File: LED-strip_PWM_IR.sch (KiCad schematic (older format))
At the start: 13 parts, among them IC1 ATtiny85, P1 CONN_2, P2 CONN_2, Q1 8MHz, T1 IRLR2905_DPAK, U1 TSOP38238, U2 7805MS

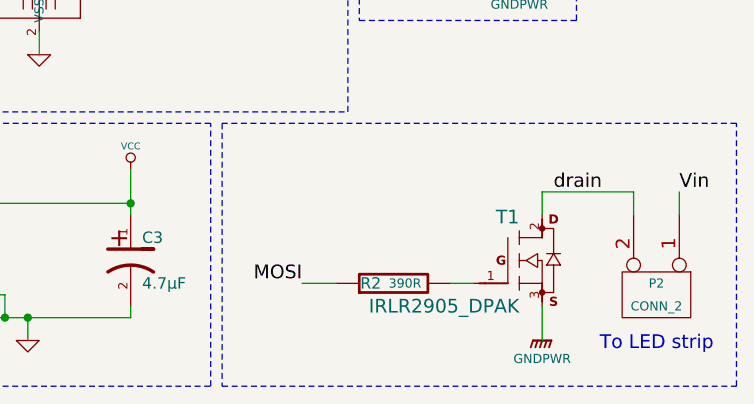
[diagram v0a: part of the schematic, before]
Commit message: Changed IRLR2905 gate resistor to 150R.
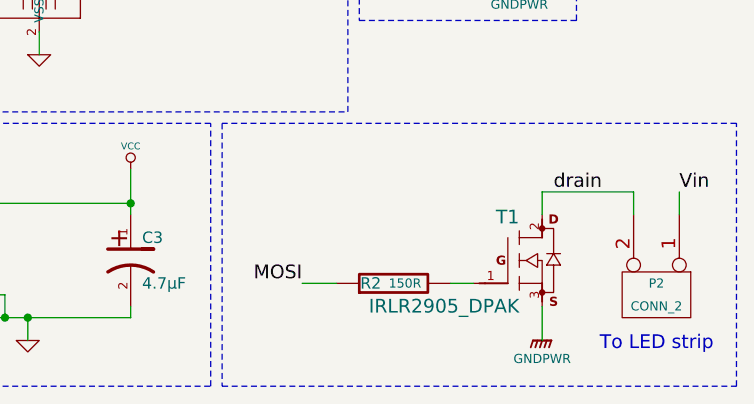
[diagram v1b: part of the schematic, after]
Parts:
- R2: value 390R -> 150R
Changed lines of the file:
@@
-EESchema Schematic File Version 2  date Sun 25 Nov 2012 02:49:51 PM CET
+EESchema Schematic File Version 2  date Mon 26 Nov 2012 02:29:05 PM CET
 LIBS:my_parts
 LIBS:power
@@
 Sheet 1 1
 Title "LED-strip_PWM_IR"
-Date "25 nov 2012"
+Date "26 nov 2012"
 Rev "0.1"
 Comp "2012 - blog.spitzenpfeil.org"
@@
 P 5350 3750
 F 0 "R2" V 5350 3850 50  0000 C CNN
-F 1 "390R" V 5350 3700 40  0000 C CNN
+F 1 "150R" V 5350 3700 40  0000 C CNN
 	1    5350 3750
 	0    -1   -1   0

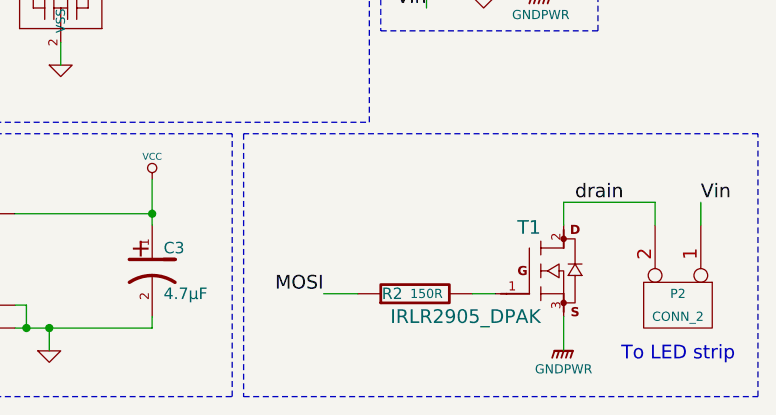
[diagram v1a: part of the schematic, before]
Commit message: Added a 20k gate pull-down.
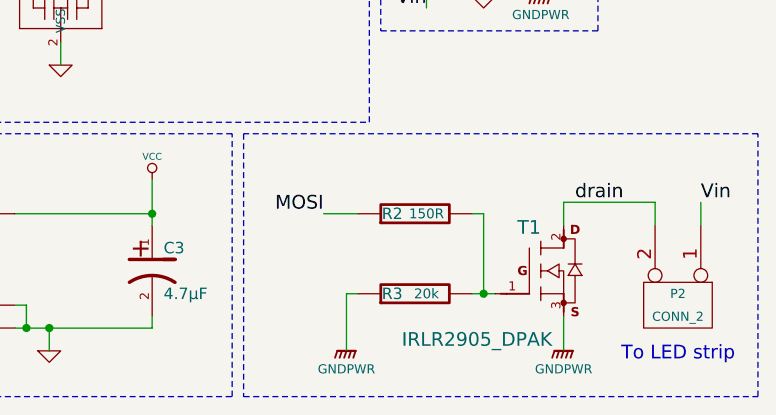
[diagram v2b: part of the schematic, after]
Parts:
- added R3: 20k, symbol R
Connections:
- net GNDPWR: now also R3.1
- net at R2.2, T1.1 (G): now also R3.2
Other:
- moved on the sheet: R2
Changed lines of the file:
@@
-EESchema Schematic File Version 2  date Mon 26 Nov 2012 02:29:05 PM CET
+EESchema Schematic File Version 2  date Tue 27 Nov 2012 09:08:00 PM CET
 LIBS:my_parts
 LIBS:power
@@
 Sheet 1 1
 Title "LED-strip_PWM_IR"
-Date "26 nov 2012"
-Rev "0.1"
+Date "27 nov 2012"
+Rev "0.11"
 Comp "2012 - blog.spitzenpfeil.org"
 Comment1 ""
@@
 L R R2
 U 1 1 4F6EEBD3
-P 5350 3750
-F 0 "R2" V 5350 3850 50  0000 C CNN
-F 1 "150R" V 5350 3700 40  0000 C CNN
-	1    5350 3750
+P 5350 3400
+F 0 "R2" V 5350 3500 50  0000 C CNN
+F 1 "150R" V 5350 3350 43  0000 C CNN
+	1    5350 3400
 	0    -1   -1   0
 $EndComp
@@
 P 5700 3750
 F 0 "T1" H 5900 4040 60  0000 R CNN
-F 1 "IRLR2905_DPAK" H 5900 3650 60  0000 R CNN
+F 1 "IRLR2905_DPAK" H 5950 3550 60  0000 R CNN
 	1    5700 3750
 	1    0    0    -1
 $EndComp
 Connection ~ 1450 1650
-Text Label 4950 3750 2    60   ~ 0
+Text Label 4950 3400 2    60   ~ 0
 MOSI
 $Comp
@@
 Wire Wire Line
 	1350 1650 1600 1650
-Wire Wire Line
-	5600 3750 5700 3750
-Wire Wire Line
-	4950 3750 5100 3750
 $Comp
 L CONN_2 P2
@@
 Text Label 6050 3350 0    60   ~ 0
 drain
+Wire Wire Line
+	4950 3400 5100 3400
+Wire Wire Line
+	5600 3400 5650 3400
+Wire Wire Line
+	5650 3400 5650 3750
+Wire Wire Line
+	5600 3750 5700 3750
+$Comp
+L R R3
+U 1 1 50B51D62
+P 5350 3750
+F 0 "R3" V 5350 3850 50  0000 C CNN
+F 1 "20k" V 5350 3700 43  0000 C CNN
+	1    5350 3750
+	0    -1   -1   0
+$EndComp
+Connection ~ 5650 3750
+Wire Wire Line
+	5100 3750 5050 3750
+Wire Wire Line
+	5050 3750 5050 4000
+$Comp
+L GNDPWR #PWR018
+U 1 1 50B51E71
+P 5050 4000
+F 0 "#PWR018" H 5050 4050 40  0001 C CNN
+F 1 "GNDPWR" H 5050 3920 40  0000 C CNN
+	1    5050 4000
+	1    0    0    -1
+$EndComp
 $EndSCHEMATC

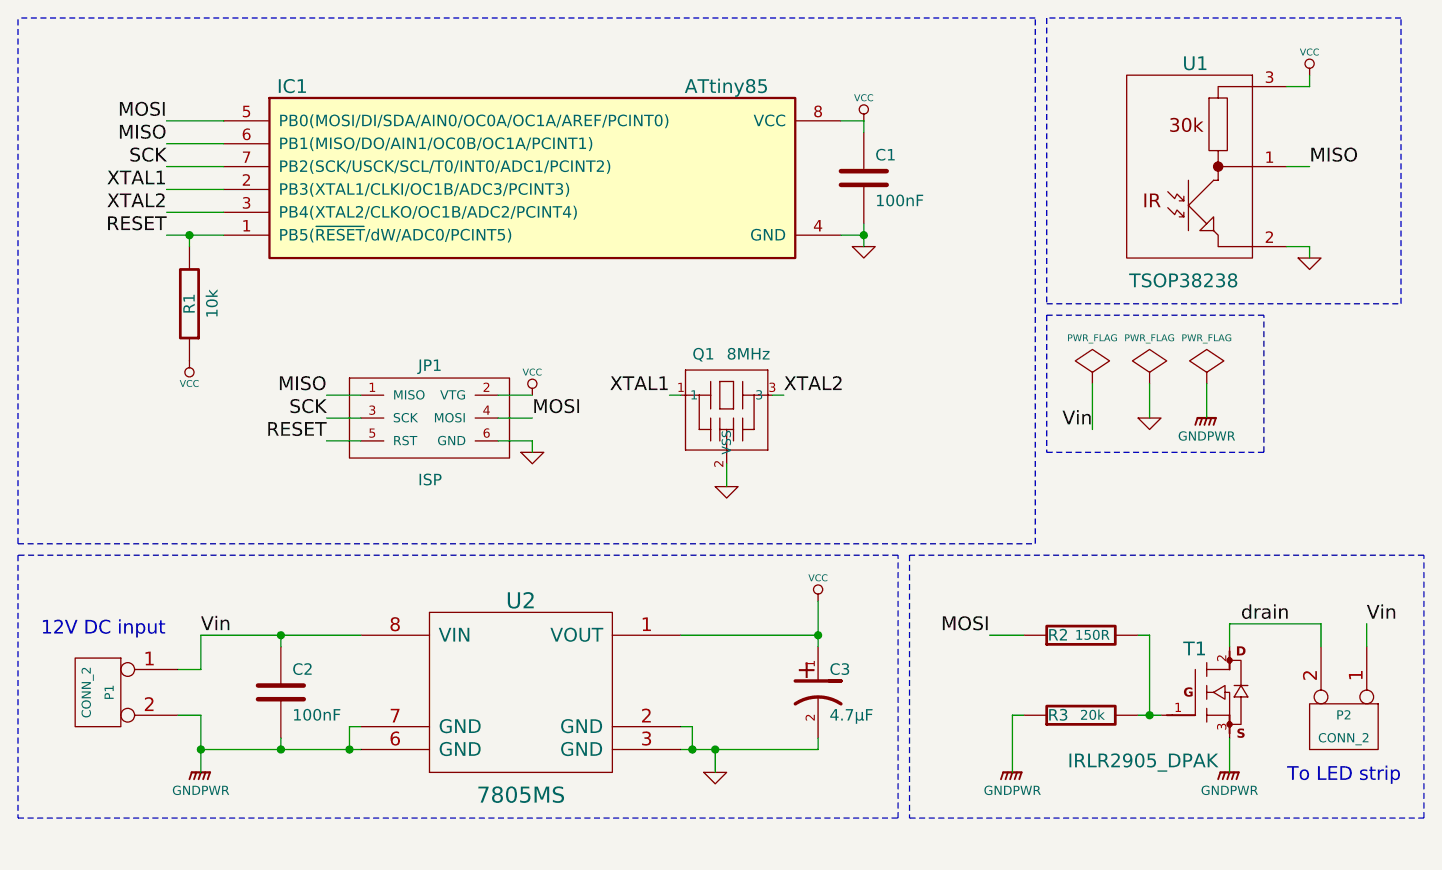
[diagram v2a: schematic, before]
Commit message: Replaced 78L05 with MCP1804-SOT23 (low drop). Board-shrink.
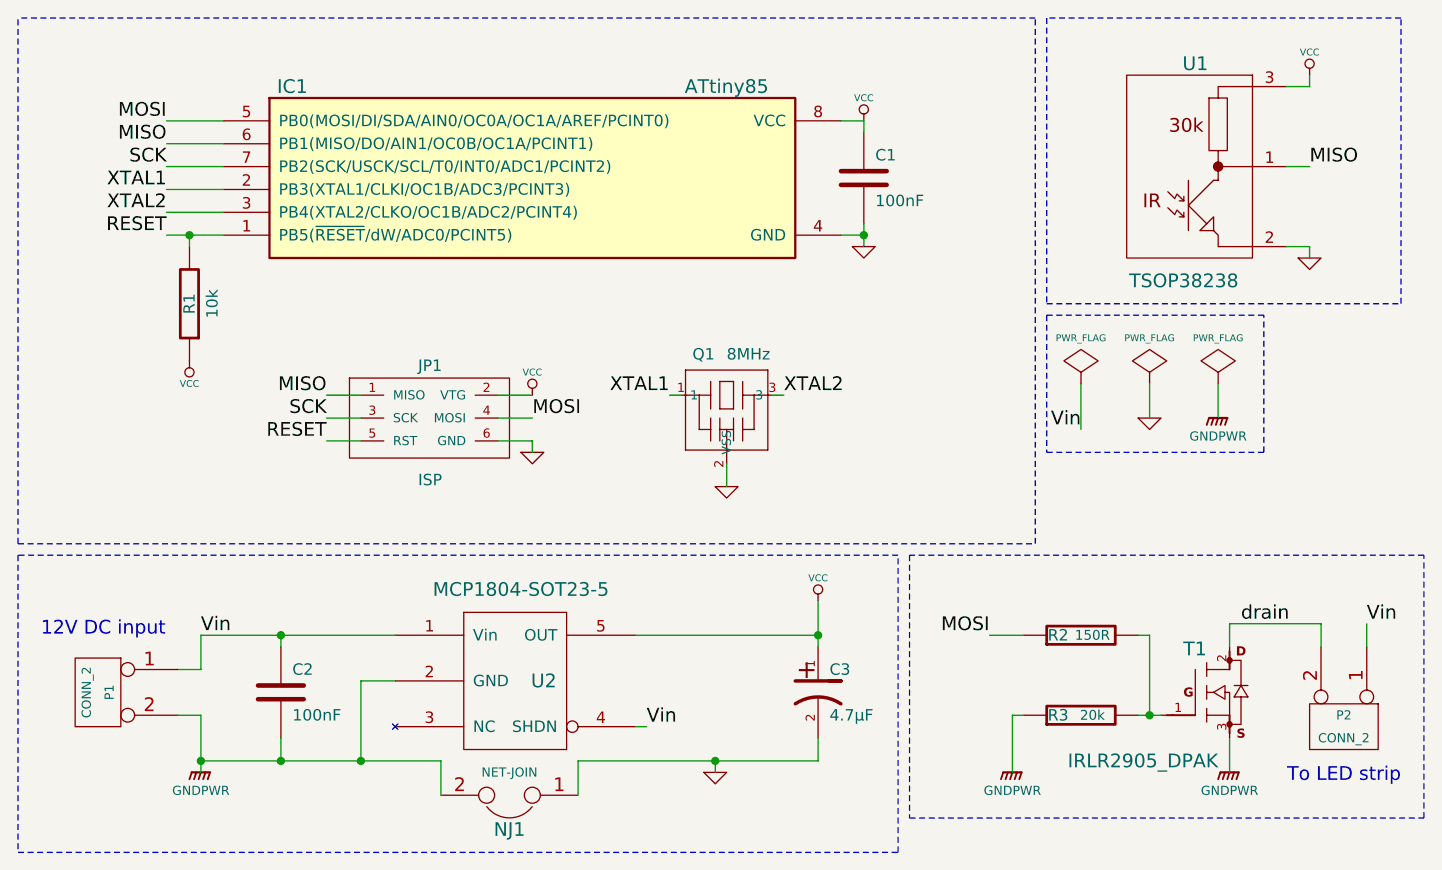
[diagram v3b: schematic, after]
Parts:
- removed U2: 7805MS, symbol 7805MS
- added NJ1: NET-JOIN, symbol JUMPER
- added U2: MCP1804-SOT23-5, symbol MADW__MCP1804-SOT23-5
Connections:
- net GND: now also NJ1.1
- net GNDPWR: now also NJ1.2, U2.2 (GND)
- net VCC: now also U2.5 (OUT)
- net Vin: now also U2.1 (Vin), U2.4 (SHDN)
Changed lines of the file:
@@
-EESchema Schematic File Version 2  date Tue 27 Nov 2012 09:08:00 PM CET
+EESchema Schematic File Version 2  date Wed 09 Jan 2013 04:06:11 PM CET
 LIBS:my_parts
 LIBS:power
@@
 EELAYER 27 0
 EELAYER END
-$Descr User 8268 5866
+$Descr User 8268 5906
 encoding utf-8
 Sheet 1 1
 Title "LED-strip_PWM_IR"
-Date "27 nov 2012"
-Rev "0.11"
+Date "9 jan 2013"
+Rev "0.2"
 Comp "2012 - blog.spitzenpfeil.org"
 Comment1 ""
@@
 	5150 700  700  700
 Wire Wire Line
-	4200 3400 3600 3400
+	3400 3400 4200 3400
 $Comp
 L VCC #PWR01
@@
 F 1 "100nF" H 1900 3550 50  0000 L CNN
 	1    1850 3650
-	1    0    0    -1
-$EndComp
-$Comp
-L PWR_FLAG #FLG02
-U 1 1 4F6EE916
-P 5650 2300
-F 0 "#FLG02" H 5650 2570 30  0001 C CNN
-F 1 "PWR_FLAG" H 5650 2500 30  0000 C CNN
-	1    5650 2300
 	1    0    0    -1
 $EndComp
@@
 RESET
 $Comp
-L GND #PWR03
+L GND #PWR02
 U 1 1 4F6EE8F0
 P 6350 1750
-F 0 "#PWR03" H 6350 1750 30  0001 C CNN
+F 0 "#PWR02" H 6350 1750 30  0001 C CNN
 F 1 "GND" H 6350 1680 30  0001 C CNN
 	1    6350 1750
@@
 $EndComp
 $Comp
-L VCC #PWR04
+L VCC #PWR03
 U 1 1 4F6EE8E3
 P 6350 950
-F 0 "#PWR04" H 6350 1050 30  0001 C CNN
+F 0 "#PWR03" H 6350 1050 30  0001 C CNN
 F 1 "VCC" H 6350 1050 30  0000 C CNN
 	1    6350 950
@@
 $EndComp
 $Comp
-L VCC #PWR05
+L VCC #PWR04
 U 1 1 4F6EE887
 P 4400 1150
-F 0 "#PWR05" H 4400 1250 30  0001 C CNN
+F 0 "#PWR04" H 4400 1250 30  0001 C CNN
 F 1 "VCC" H 4400 1250 30  0000 C CNN
 	1    4400 1150
@@
 $EndComp
 $Comp
-L GND #PWR06
+L GND #PWR05
 U 1 1 4F6EE882
 P 4400 1700
-F 0 "#PWR06" H 4400 1700 30  0001 C CNN
+F 0 "#PWR05" H 4400 1700 30  0001 C CNN
 F 1 "GND" H 4400 1630 30  0001 C CNN
 	1    4400 1700
@@
 MOSI
 $Comp
-L GND #PWR07
+L GND #PWR06
 U 1 1 4F6EE81E
 P 2950 2600
-F 0 "#PWR07" H 2950 2600 30  0001 C CNN
+F 0 "#PWR06" H 2950 2600 30  0001 C CNN
 F 1 "GND" H 2950 2530 30  0001 C CNN
 	1    2950 2600
@@
 MOSI
 $Comp
-L VCC #PWR08
+L VCC #PWR07
 U 1 1 4F6EE80A
 P 2950 2350
-F 0 "#PWR08" H 2950 2450 30  0001 C CNN
+F 0 "#PWR07" H 2950 2450 30  0001 C CNN
 F 1 "VCC" H 2950 2450 30  0000 C CNN
 	1    2950 2350
@@
 XTAL2
 $Comp
-L GND #PWR09
+L GND #PWR08
 U 1 1 4F6EE7AB
 P 3800 2750
-F 0 "#PWR09" H 3800 2750 30  0001 C CNN
+F 0 "#PWR08" H 3800 2750 30  0001 C CNN
 F 1 "GND" H 3800 2680 30  0001 C CNN
 	1    3800 2750
@@
 $EndComp
 $Comp
-L VCC #PWR010
+L VCC #PWR09
 U 1 1 4F6EE70F
 P 1450 2200
-F 0 "#PWR010" H 1450 2300 30  0001 C CNN
+F 0 "#PWR09" H 1450 2300 30  0001 C CNN
 F 1 "VCC" H 1450 2300 30  0000 C CNN
 	1    1450 2200
@@
 $EndComp
 $Comp
-L PWR_FLAG #FLG011
+L PWR_FLAG #FLG010
 U 1 1 50B1E380
-P 5400 2300
-F 0 "#FLG011" H 5400 2395 30  0001 C CNN
-F 1 "PWR_FLAG" H 5400 2500 30  0000 C CNN
-	1    5400 2300
-	1    0    0    -1
-$EndComp
-$Comp
-L 7805MS U2
-U 1 1 50B1E462
-P 2900 3650
-F 0 "U2" H 2900 4050 70  0000 C CNN
-F 1 "7805MS" H 2900 3200 70  0000 C CNN
-	1    2900 3650
-	1    0    0    -1
-$EndComp
-Wire Wire Line
-	1500 3900 2200 3900
-Wire Wire Line
-	2200 3800 2150 3800
-Wire Wire Line
-	2150 3800 2150 3900
-Connection ~ 2150 3900
-Wire Wire Line
-	3600 3900 4200 3900
-Connection ~ 3650 3900
+P 5350 2300
+F 0 "#FLG010" H 5350 2395 30  0001 C CNN
+F 1 "PWR_FLAG" H 5350 2500 30  0000 C CNN
+	1    5350 2300
+	1    0    0    -1
+$EndComp
 Connection ~ 4200 3400
 Wire Wire Line
-	4200 3900 4200 3850
-Wire Notes Line
-	4550 4200 4550 3050
+	4200 3950 4200 3850
 $Comp
 L MADW__IRLZ34N T1
@@
 MOSI
 $Comp
-L GNDPWR #PWR012
+L GNDPWR #PWR011
 U 1 1 50B209CF
 P 6000 4000
-F 0 "#PWR012" H 6000 4050 40  0001 C CNN
+F 0 "#PWR011" H 6000 4050 40  0001 C CNN
 F 1 "GNDPWR" H 6000 3920 40  0000 C CNN
 	1    6000 4000
@@
 	6750 1950 6750 700
 Wire Wire Line
-	1500 3400 2200 3400
+	1500 3400 2350 3400
 Wire Wire Line
 	1400 3750 1500 3750
 Wire Wire Line
 	1500 3750 1500 4000
-Connection ~ 1850 3900
 Wire Wire Line
 	1400 3550 1500 3550
@@
 	1500 3550 1500 3400
 Connection ~ 1850 3400
-Connection ~ 1500 3900
-$Comp
-L GND #PWR013
-U 1 1 50B21224
-P 3750 4000
-F 0 "#PWR013" H 3750 4000 30  0001 C CNN
-F 1 "GND" H 3750 3930 30  0001 C CNN
-	1    3750 4000
-	1    0    0    -1
-$EndComp
-Wire Wire Line
-	3600 3800 3650 3800
-Wire Wire Line
-	3650 3800 3650 3900
 Wire Wire Line
 	1850 3450 1850 3400
 Wire Wire Line
-	1850 3900 1850 3850
+	1850 3850 1850 3950
+$Comp
+L GNDPWR #PWR012
+U 1 1 50B2137E
+P 5950 2450
+F 0 "#PWR012" H 5950 2500 40  0001 C CNN
+F 1 "GNDPWR" H 5950 2370 40  0000 C CNN
+	1    5950 2450
+	1    0    0    -1
+$EndComp
+Wire Notes Line
+	4550 3050 700  3050
+$Comp
+L PWR_FLAG #FLG013
+U 1 1 50B2144E
+P 5950 2300
+F 0 "#FLG013" H 5950 2395 30  0001 C CNN
+F 1 "PWR_FLAG" H 5950 2500 30  0000 C CNN
+	1    5950 2300
+	1    0    0    -1
+$EndComp
+Text Label 5350 2500 2    60   ~ 0
+Vin
+Wire Wire Line
+	5950 2300 5950 2450
+Wire Wire Line
+	5350 2300 5350 2500
+Wire Notes Line
+	5200 2000 5200 2600
+Wire Notes Line
+	5200 2600 6150 2600
+Wire Notes Line
+	6150 2600 6150 2000
+Wire Notes Line
+	6150 2000 5200 2000
 $Comp
 L GNDPWR #PWR014
-U 1 1 50B2137E
-P 5900 2450
-F 0 "#PWR014" H 5900 2500 40  0001 C CNN
-F 1 "GNDPWR" H 5900 2370 40  0000 C CNN
-	1    5900 2450
-	1    0    0    -1
-$EndComp
-Wire Notes Line
-	4550 3050 700  3050
-Wire Notes Line
-	700  3050 700  4200
-Wire Notes Line
-	700  4200 4550 4200
-$Comp
-L PWR_FLAG #FLG015
-U 1 1 50B2144E
-P 5900 2300
-F 0 "#FLG015" H 5900 2395 30  0001 C CNN
-F 1 "PWR_FLAG" H 5900 2500 30  0000 C CNN
-	1    5900 2300
-	1    0    0    -1
-$EndComp
-$Comp
-L GND #PWR016
-U 1 1 50B2147B
-P 5650 2450
-F 0 "#PWR016" H 5650 2450 30  0001 C CNN
-F 1 "GND" H 5650 2380 30  0001 C CNN
-	1    5650 2450
-	1    0    0    -1
-$EndComp
-Text Label 5400 2500 2    60   ~ 0
-Vin
-Wire Wire Line
-	5900 2300 5900 2450
-Wire Wire Line
-	5650 2300 5650 2450
-Wire Wire Line
-	5400 2300 5400 2500
-Wire Notes Line
-	5200 2000 5200 2600
-Wire Notes Line
-	5200 2600 6150 2600
-Wire Notes Line
-	6150 2600 6150 2000
-Wire Notes Line
-	6150 2000 5200 2000
-$Comp
-L GNDPWR #PWR017
 U 1 1 50B216E0
 P 1500 4000
-F 0 "#PWR017" H 1500 4050 40  0001 C CNN
+F 0 "#PWR014" H 1500 4050 40  0001 C CNN
 F 1 "GNDPWR" H 1500 3920 40  0000 C CNN
 	1    1500 4000
 	1    0    0    -1
 $EndComp
-Wire Wire Line
-	3750 3900 3750 4000
-Connection ~ 3750 3900
 Text Label 6050 3350 0    60   ~ 0
 drain
@@
 	5050 3750 5050 4000
 $Comp
-L GNDPWR #PWR018
+L GNDPWR #PWR015
 U 1 1 50B51E71
 P 5050 4000
-F 0 "#PWR018" H 5050 4050 40  0001 C CNN
+F 0 "#PWR015" H 5050 4050 40  0001 C CNN
 F 1 "GNDPWR" H 5050 3920 40  0000 C CNN
 	1    5050 4000
 	1    0    0    -1
 $EndComp
+$Comp
+L MADW__MCP1804-SOT23-5 U2
+U 1 1 50ED7AA4
+P 2850 3600
+F 0 "U2" H 3000 3600 60  0000 C CNN
+F 1 "MCP1804-SOT23-5" H 2900 4000 60  0000 C CNN
+	1    2850 3600
+	1    0    0    -1
+$EndComp
+Connection ~ 1500 3950
+Wire Wire Line
+	2350 3600 2200 3600
+Wire Wire Line
+	2200 3600 2200 3950
+Connection ~ 2200 3950
+Connection ~ 1850 3950
+Connection ~ 3750 3950
+$Comp
+L GND #PWR016
+U 1 1 50B21224
+P 3750 4000
+F 0 "#PWR016" H 3750 4000 30  0001 C CNN
+F 1 "GND" H 3750 3930 30  0001 C CNN
+	1    3750 4000
+	1    0    0    -1
+$EndComp
+Wire Wire Line
+	3750 3950 3750 4000
+Text Label 3450 3800 0    60   ~ 0
+Vin
+Wire Wire Line
+	3400 3800 3450 3800
+$Comp
+L JUMPER NJ1
+U 1 1 50ED7F02
+P 2850 4100
+F 0 "NJ1" H 2850 4250 60  0000 C CNN
+F 1 "NET-JOIN" H 2850 4000 40  0000 C CNN
+	1    2850 4100
+	-1   0    0    1
+$EndComp
+Wire Wire Line
+	1500 3950 2550 3950
+Wire Wire Line
+	2550 3950 2550 4100
+Wire Wire Line
+	3150 4100 3150 3950
+Wire Wire Line
+	3150 3950 4200 3950
+Wire Notes Line
+	700  3050 700  4350
+Wire Notes Line
+	700  4350 4550 4350
+Wire Notes Line
+	4550 4350 4550 3050
+$Comp
+L PWR_FLAG #FLG017
+U 1 1 50ED815F
+P 5650 2300
+F 0 "#FLG017" H 5650 2395 30  0001 C CNN
+F 1 "PWR_FLAG" H 5650 2500 30  0000 C CNN
+	1    5650 2300
+	1    0    0    -1
+$EndComp
+Wire Wire Line
+	5650 2300 5650 2450
+$Comp
+L GND #PWR018
+U 1 1 50ED8167
+P 5650 2450
+F 0 "#PWR018" H 5650 2450 30  0001 C CNN
+F 1 "GND" H 5650 2380 30  0001 C CNN
+	1    5650 2450
+	1    0    0    -1
+$EndComp
